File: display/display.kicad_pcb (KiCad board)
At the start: 2 copper layers, 80 x 20 mm, 49 parts, among them P1 CONN_6, P2 CONN_8

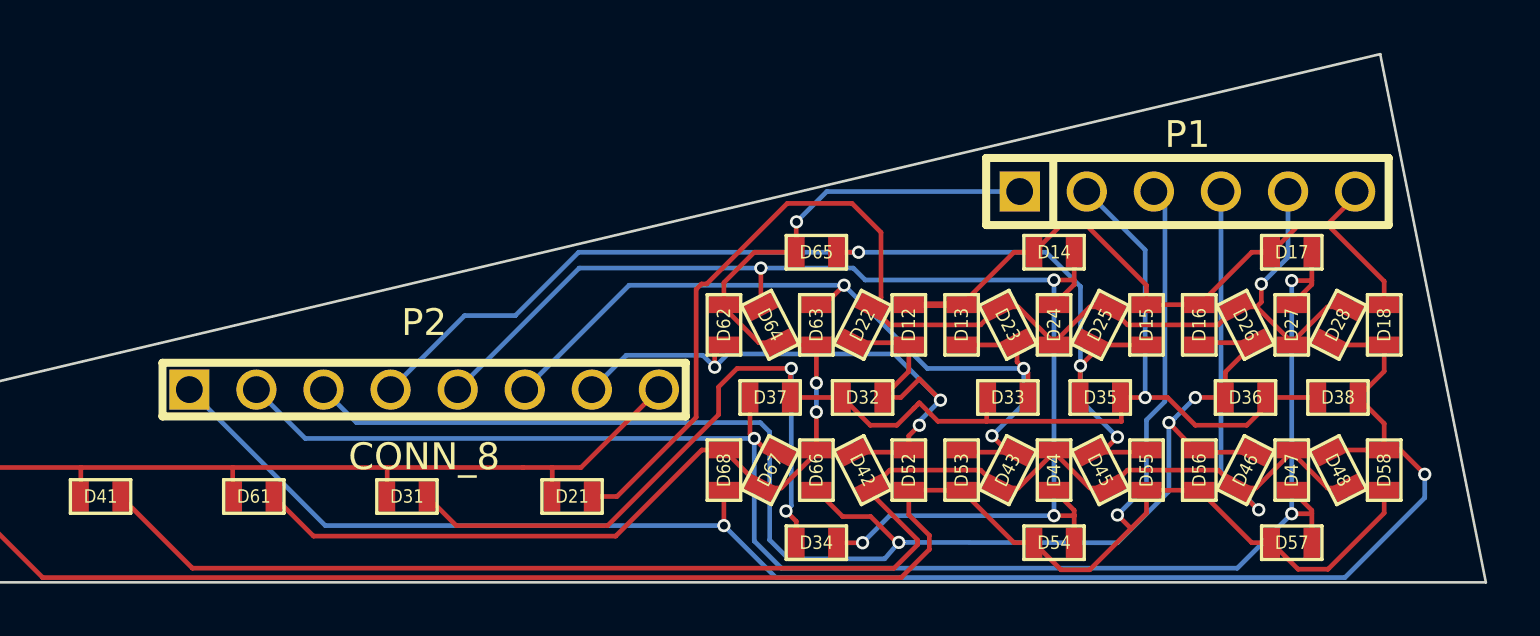
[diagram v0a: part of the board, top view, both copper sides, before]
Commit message: Remove pin headers.
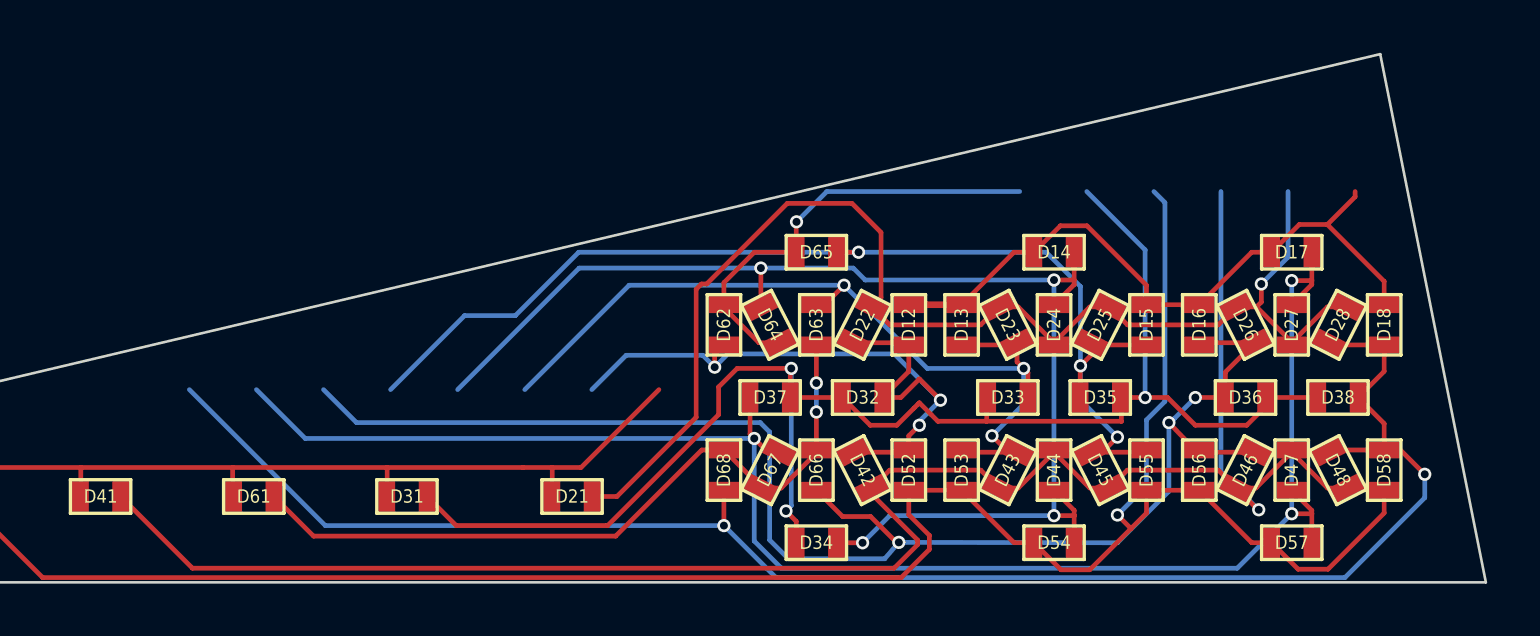
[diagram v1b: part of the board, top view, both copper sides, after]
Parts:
- removed P1: CONN_6, PIN_ARRAY-6X1
- removed P2: CONN_8, pin_array_8x1
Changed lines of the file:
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@@
 (kicad_pcb (version 3) (host pcbnew "(2013-mar-13)-testing")
   (general
-    (links 94)
+    (links 80)
     (no_connects 0)
     (area 102.35 82.69 182.741571 109.132371)
@@
     (tracks 356)
     (zones 0)
-    (modules 49)
+    (modules 47)
     (nets 15)
   )
@@
     (mod_text_size 1.524 1.524)
     (mod_text_width 0.3048)
-    (pad_size 1.524 1.524)
-    (pad_drill 0.8128)
+    (pad_size 0.8 0.8)
+    (pad_drill 0)
     (pad_to_mask_clearance 0.254)
     (aux_axis_origin 0 0)
@@
       (rotate (xyz 0 0 0))
     )
-  )
-  (module PIN_ARRAY-6X1 (layer Front)
-    (at 171.39158 94.2848)
-    (descr "Connecteur 6 pins")
-    (tags "CONN DEV")
-    (fp_text reference P1 (at 0 -2.159) (layer F.SilkS)
-      (effects (font (size 1.016 1.016) (thickness 0.2032)))
-    )
-    (fp_text value CONN_6 (at 0 2.159) (layer F.SilkS) hide
-      (effects (font (size 1.016 0.889) (thickness 0.2032)))
-    )
-    (fp_line (start -7.62 1.27) (end -7.62 -1.27) (layer F.SilkS) (width 0.3048))
-    (fp_line (start -7.62 -1.27) (end 7.62 -1.27) (layer F.SilkS) (width 0.3048))
-    (fp_line (start 7.62 -1.27) (end 7.62 1.27) (layer F.SilkS) (width 0.3048))
-    (fp_line (start 7.62 1.27) (end -7.62 1.27) (layer F.SilkS) (width 0.3048))
-    (fp_line (start -5.08 1.27) (end -5.08 -1.27) (layer F.SilkS) (width 0.3048))
-    (pad 1 thru_hole rect (at -6.35 0) (size 1.524 1.524) (drill 1.016)
-      (layers *.Cu *.Mask F.SilkS)
-      (net 14 /ROW6)
-    )
-    (pad 2 thru_hole circle (at -3.81 0) (size 1.524 1.524) (drill 1.016)
-      (layers *.Cu *.Mask F.SilkS)
-      (net 11 /ROW3)
-    )
-    (pad 3 thru_hole circle (at -1.27 0) (size 1.524 1.524) (drill 1.016)
-      (layers *.Cu *.Mask F.SilkS)
-      (net 13 /ROW5)
-    )
-    (pad 4 thru_hole circle (at 1.27 0) (size 1.524 1.524) (drill 1.016)
-      (layers *.Cu *.Mask F.SilkS)
-      (net 12 /ROW4)
-    )
-    (pad 5 thru_hole circle (at 3.81 0) (size 1.524 1.524) (drill 1.016)
-      (layers *.Cu *.Mask F.SilkS)
-      (net 10 /ROW2)
-    )
-    (pad 6 thru_hole circle (at 6.35 0) (size 1.524 1.524) (drill 1.016)
-      (layers *.Cu *.Mask F.SilkS)
-      (net 9 /ROW1)
-    )
-    (model pin_array/pins_array_6x1.wrl
-      (at (xyz 0 0 0))
-      (scale (xyz 1 1 1))
-      (rotate (xyz 0 0 0))
-    )
-  )
-  (module pin_array_8x1 (layer Front)
-    (at 142.49146 101.78542)
-    (descr "8x1 pin array")
-    (tags CONN)
-    (fp_text reference P2 (at 0 -2.54) (layer F.SilkS)
-      (effects (font (size 1.016 1.016) (thickness 0.2032)))
-    )
-    (fp_text value CONN_8 (at 0 2.54) (layer F.SilkS)
-      (effects (font (size 1.016 1.016) (thickness 0.2032)))
-    )
-    (fp_line (start -9.906 1.016) (end -9.906 -1.016) (layer F.SilkS) (width 0.3048))
-    (fp_line (start -9.906 -1.016) (end 9.906 -1.016) (layer F.SilkS) (width 0.3048))
-    (fp_line (start 9.906 -1.016) (end 9.906 1.016) (layer F.SilkS) (width 0.3048))
-    (fp_line (start 9.906 1.016) (end -9.906 1.016) (layer F.SilkS) (width 0.3048))
-    (pad 1 thru_hole rect (at -8.89 0) (size 1.524 1.524) (drill 1.016)
-      (layers *.Cu *.Mask F.SilkS)
-      (net 8 /COL8)
-    )
-    (pad 2 thru_hole circle (at -6.35 0) (size 1.524 1.524) (drill 1.016)
-      (layers *.Cu *.Mask F.SilkS)
-      (net 7 /COL7)
-    )
-    (pad 3 thru_hole circle (at -3.81 0) (size 1.524 1.524) (drill 1.016)
-      (layers *.Cu *.Mask F.SilkS)
-      (net 6 /COL6)
-    )
-    (pad 4 thru_hole circle (at -1.27 0) (size 1.524 1.524) (drill 1.016)
-      (layers *.Cu *.Mask F.SilkS)
-      (net 5 /COL5)
-    )
-    (pad 5 thru_hole circle (at 1.27 0) (size 1.524 1.524) (drill 1.016)
-      (layers *.Cu *.Mask F.SilkS)
-      (net 4 /COL4)
-    )
-    (pad 6 thru_hole circle (at 3.81 0) (size 1.524 1.524) (drill 1.016)
-      (layers *.Cu *.Mask F.SilkS)
-      (net 3 /COL3)
-    )
-    (pad 7 thru_hole circle (at 6.35 0) (size 1.524 1.524) (drill 1.016)
-      (layers *.Cu *.Mask F.SilkS)
-      (net 2 /COL2)
-    )
-    (pad 8 thru_hole circle (at 8.89 0) (size 1.524 1.524) (drill 1.016)
-      (layers *.Cu *.Mask F.SilkS)
-      (net 1 /COL1)
-    )
-    (model pin_array/pins_array_8x2.wrl
-      (at (xyz 0 0 0))
-      (scale (xyz 1 1 1))
-      (rotate (xyz 0 0 0))
-    )

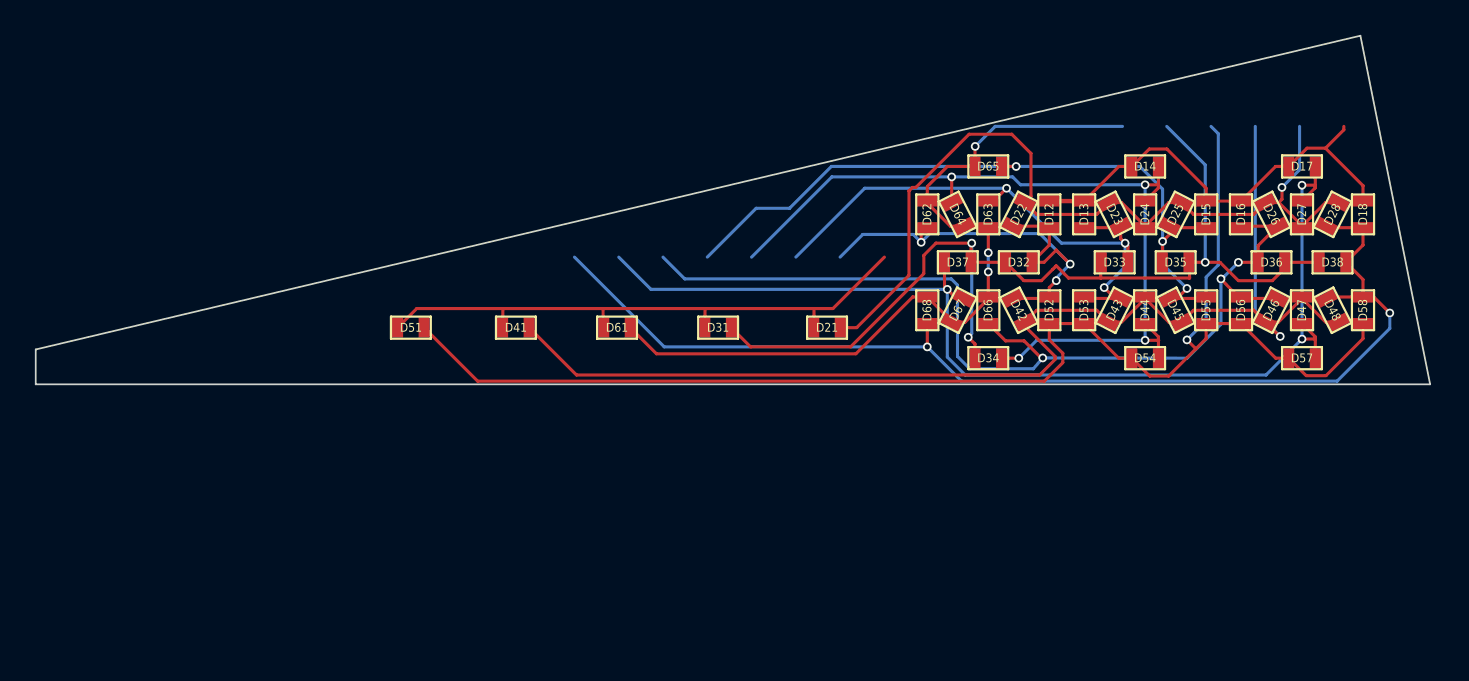
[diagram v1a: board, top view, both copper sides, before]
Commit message: Update netlist and board to use the new connector and diode footprints.
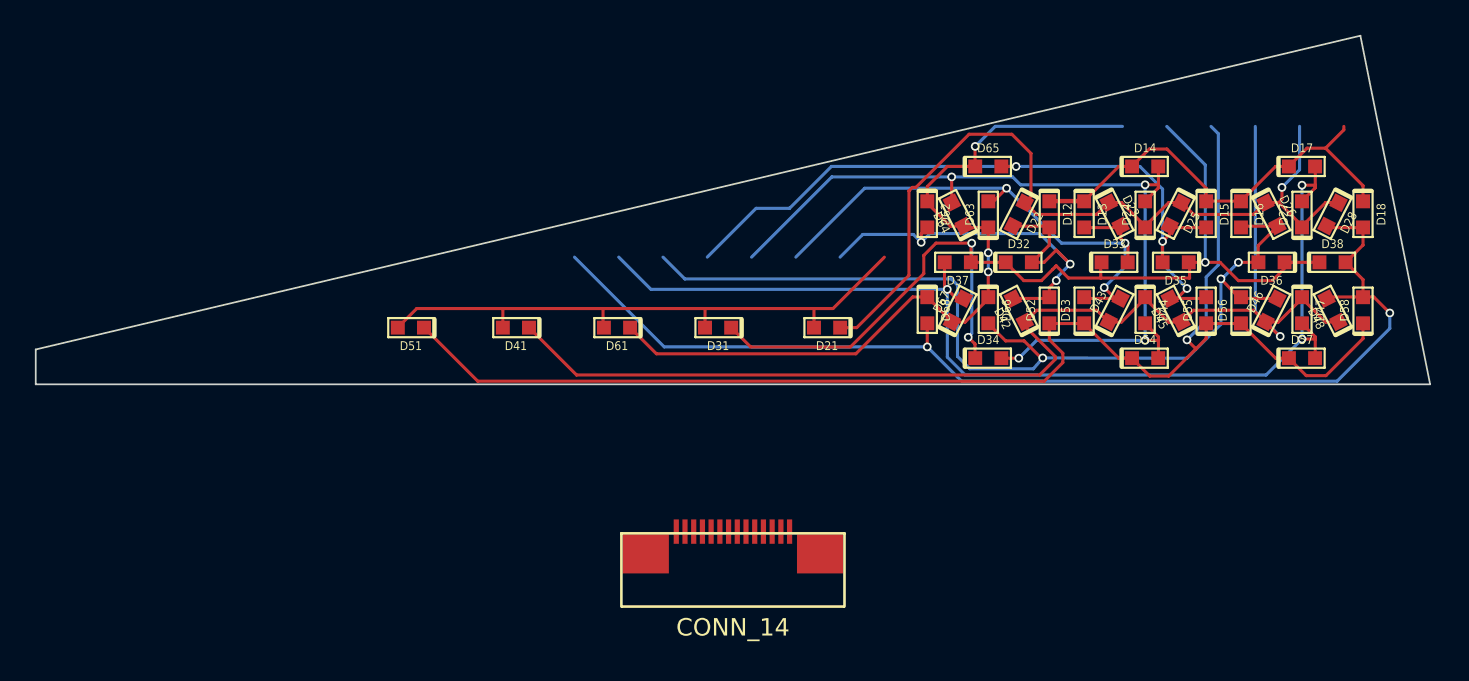
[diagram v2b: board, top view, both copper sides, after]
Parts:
- added P1: CONN_14, SFV14R-2STE1HLF, F.Cu at (142.7, 121.8)
- D12, D13, D14, D15, D16, D17, D18, D21, D22, D23, D24, D25, D26, D27, D28, D31, D32, D33, D34, D35, D36, D37, D38, D41, D42, D43, D44, D45, D46, D47, D48, D51, D52, D53, D54, D55, D56, D57, D58, D61, D62, D63, D64, D65, D66, D67, D68: value DIODE -> LED; footprint SM0603 -> SM0603_Diode
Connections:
- D12 pad 1: /ROW1 -> (no net)
- D12 pad 2: /COL2 -> (no net)
- D13 pad 1: /ROW1 -> (no net)
- D13 pad 2: /COL3 -> (no net)
- D14 pad 1: /ROW1 -> (no net)
- D14 pad 2: /COL4 -> (no net)
- D15 pad 1: /ROW1 -> (no net)
- D15 pad 2: /COL5 -> (no net)
- D16 pad 1: /ROW1 -> (no net)
- D16 pad 2: /COL6 -> (no net)
- D17 pad 1: /ROW1 -> (no net)
- D17 pad 2: /COL7 -> (no net)
- D18 pad 1: /ROW1 -> (no net)
- D18 pad 2: /COL8 -> (no net)
- D21 pad 1: /ROW2 -> (no net)
- D21 pad 2: /COL1 -> (no net)
- D22 pad 1: /ROW2 -> (no net)
- D22 pad 2: /COL2 -> (no net)
- D23 pad 1: /ROW2 -> (no net)
- D23 pad 2: /COL3 -> (no net)
- D24 pad 1: /ROW2 -> (no net)
- D24 pad 2: /COL4 -> (no net)
- D25 pad 1: /ROW2 -> (no net)
- D25 pad 2: /COL5 -> (no net)
- D26 pad 1: /ROW2 -> (no net)
- D26 pad 2: /COL6 -> (no net)
- D27 pad 1: /ROW2 -> (no net)
- D27 pad 2: /COL7 -> (no net)
- D28 pad 1: /ROW2 -> (no net)
- D28 pad 2: /COL8 -> (no net)
- D31 pad 1: /ROW3 -> (no net)
- D31 pad 2: /COL1 -> (no net)
- D32 pad 1: /ROW3 -> (no net)
- D32 pad 2: /COL2 -> (no net)
- D33 pad 1: /ROW3 -> (no net)
- D33 pad 2: /COL3 -> (no net)
- D34 pad 1: /ROW3 -> (no net)
- D34 pad 2: /COL4 -> (no net)
- D35 pad 1: /ROW3 -> (no net)
- D35 pad 2: /COL5 -> (no net)
- D36 pad 1: /ROW3 -> (no net)
- D36 pad 2: /COL6 -> (no net)
- D37 pad 1: /ROW3 -> (no net)
- D37 pad 2: /COL7 -> (no net)
- D38 pad 1: /ROW3 -> (no net)
- D38 pad 2: /COL8 -> (no net)
- D41 pad 1: /ROW4 -> (no net)
- D41 pad 2: /COL1 -> (no net)
- D42 pad 1: /ROW4 -> (no net)
- D42 pad 2: /COL2 -> (no net)
- D43 pad 1: /ROW4 -> (no net)
- D43 pad 2: /COL3 -> (no net)
- D44 pad 1: /ROW4 -> (no net)
- D44 pad 2: /COL4 -> (no net)
- D45 pad 1: /ROW4 -> (no net)
- D45 pad 2: /COL5 -> (no net)
- D46 pad 1: /ROW4 -> (no net)
- D46 pad 2: /COL6 -> (no net)
- D47 pad 1: /ROW4 -> (no net)
- D47 pad 2: /COL7 -> (no net)
- D48 pad 1: /ROW4 -> (no net)
- D48 pad 2: /COL8 -> (no net)
- D51 pad 1: /ROW5 -> (no net)
- D51 pad 2: /COL1 -> (no net)
- D52 pad 1: /ROW5 -> (no net)
- D52 pad 2: /COL2 -> (no net)
- D53 pad 1: /ROW5 -> (no net)
- D53 pad 2: /COL3 -> (no net)
- D54 pad 1: /ROW5 -> (no net)
- D54 pad 2: /COL4 -> (no net)
- D55 pad 1: /ROW5 -> (no net)
- D55 pad 2: /COL5 -> (no net)
- D56 pad 1: /ROW5 -> (no net)
- D56 pad 2: /COL6 -> (no net)
- D57 pad 1: /ROW5 -> (no net)
- D57 pad 2: /COL7 -> (no net)
- D58 pad 1: /ROW5 -> (no net)
- D58 pad 2: /COL8 -> (no net)
- D61 pad 1: /ROW6 -> (no net)
- D61 pad 2: /COL1 -> (no net)
- D62 pad 1: /ROW6 -> (no net)
- D62 pad 2: /COL2 -> (no net)
- D63 pad 1: /ROW6 -> (no net)
- D63 pad 2: /COL3 -> (no net)
- D64 pad 1: /ROW6 -> (no net)
- D64 pad 2: /COL4 -> (no net)
- D65 pad 1: /ROW6 -> (no net)
- D65 pad 2: /COL5 -> (no net)
- D66 pad 1: /ROW6 -> (no net)
- D66 pad 2: /COL6 -> (no net)
- D67 pad 1: /ROW6 -> (no net)
- D67 pad 2: /COL7 -> (no net)
- D68 pad 1: /ROW6 -> (no net)
- D68 pad 2: /COL8 -> (no net)
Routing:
- net (no net): track 0.00 -> 699.0 mm, vias 0 -> 30
- net /ROW5: track 78.8 -> 0.00 mm, vias 1 -> 0
- net /ROW4: track 70.1 -> 0.00 mm, vias 1 -> 0
- net /COL8: track 64.2 -> 0.00 mm, vias 2 -> 0
- net /COL7: track 62.9 -> 0.00 mm, vias 3 -> 0
- net /ROW3: track 58.1 -> 0.00 mm, vias 3 -> 0
- net /COL6: track 55.6 -> 0.00 mm, vias 3 -> 0
- net /COL4: track 49.9 -> 0.00 mm, vias 4 -> 0
- net /ROW2: track 48.4 -> 0.00 mm, vias 1 -> 0
- net /ROW6: track 46.1 -> 0.00 mm, vias 3 -> 0
- net /COL5: track 43.7 -> 0.00 mm, vias 3 -> 0
- net /COL1: track 34.0 -> 0.00 mm
- net /COL3: track 33.9 -> 0.00 mm, vias 3 -> 0
- net /COL2: track 27.7 -> 0.00 mm, vias 3 -> 0
- net /ROW1: track 25.6 -> 0.00 mm
